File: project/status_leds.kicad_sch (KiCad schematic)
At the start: 12 parts

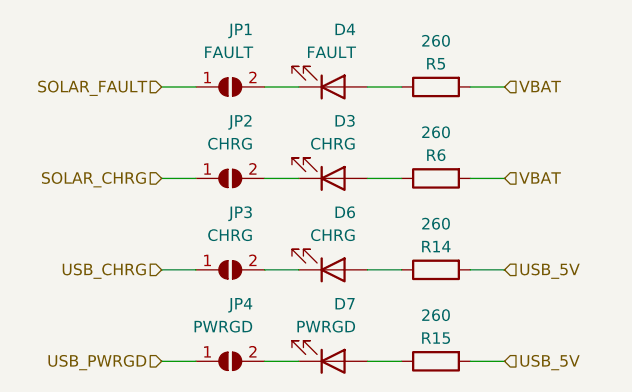
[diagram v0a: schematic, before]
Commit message: Added symbol annotations
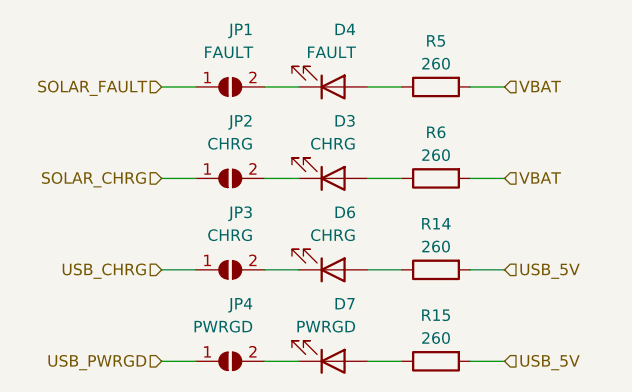
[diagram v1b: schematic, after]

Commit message: Minor improvements
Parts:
- R14, R15: value 260 -> 500
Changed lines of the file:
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@@
       (effects (font (size 1.27 1.27)))
     )
-    (property "Value" "260" (at 157.48 106.68 90)
+    (property "Value" "500" (at 157.48 106.68 90)
       (effects (font (size 1.27 1.27)))
     )
@@
       (effects (font (size 1.27 1.27)))
     )
-    (property "Value" "260" (at 157.48 96.52 90)
+    (property "Value" "500" (at 157.48 96.52 90)
       (effects (font (size 1.27 1.27)))
     )

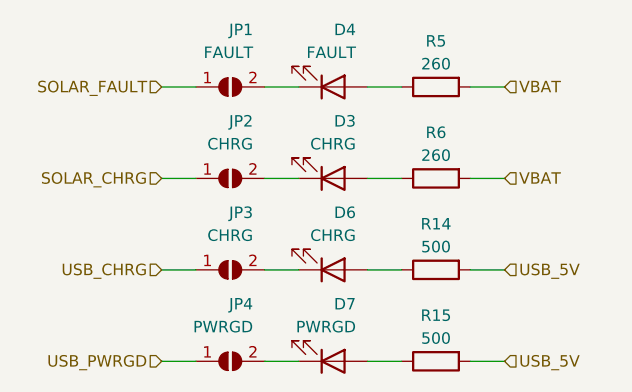
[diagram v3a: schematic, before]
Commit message: Fixed solar status LEDs wrong VBAT
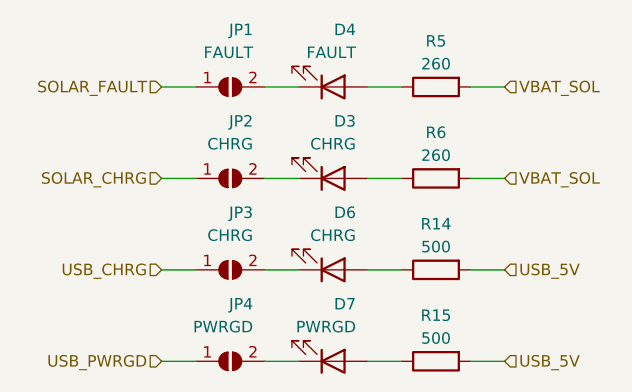
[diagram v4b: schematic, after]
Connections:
- net VBAT renamed VBAT_SOL
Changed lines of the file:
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@@
     (effects (font (size 1.27 1.27)) (justify left))
   )
-  (hierarchical_label "VBAT" (shape input) (at 165.1 88.9 0) (fields_autoplaced)
+  (hierarchical_label "VBAT_SOL" (shape input) (at 165.1 88.9 0) (fields_autoplaced)
     (effects (font (size 1.27 1.27)) (justify left))
   )
@@
     (effects (font (size 1.27 1.27)) (justify left))
   )
-  (hierarchical_label "VBAT" (shape input) (at 165.1 78.74 0) (fields_autoplaced)
+  (hierarchical_label "VBAT_SOL" (shape input) (at 165.1 78.74 0) (fields_autoplaced)
     (effects (font (size 1.27 1.27)) (justify left))
   )

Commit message: Dimmed the USB status LEDs (again)
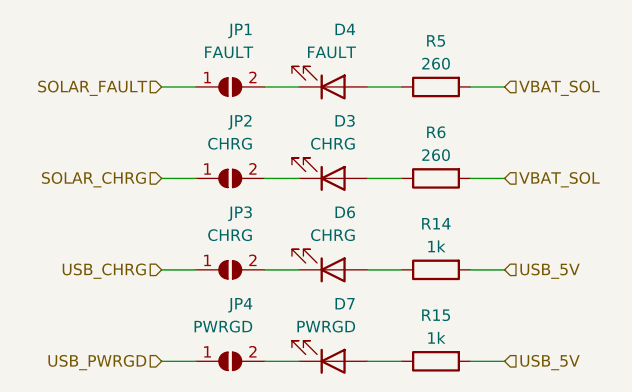
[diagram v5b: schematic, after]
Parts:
- R14, R15: value 500 -> 1k
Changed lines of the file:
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@@
       (effects (font (size 1.27 1.27)))
     )
-    (property "Value" "500" (at 157.48 106.68 90)
+    (property "Value" "1k" (at 157.48 106.68 90)
       (effects (font (size 1.27 1.27)))
     )
@@
       (effects (font (size 1.27 1.27)))
     )
-    (property "Value" "500" (at 157.48 96.52 90)
+    (property "Value" "1k" (at 157.48 96.52 90)
       (effects (font (size 1.27 1.27)))
     )

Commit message: Final revision
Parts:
- renumbered D3 to D5, JP1 to JP2, JP2 to JP3, JP3 to JP4, JP4 to JP5, R5 to R16, R6 to R17, R14 to R18, R15 to R19
